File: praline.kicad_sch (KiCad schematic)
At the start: 0 parts

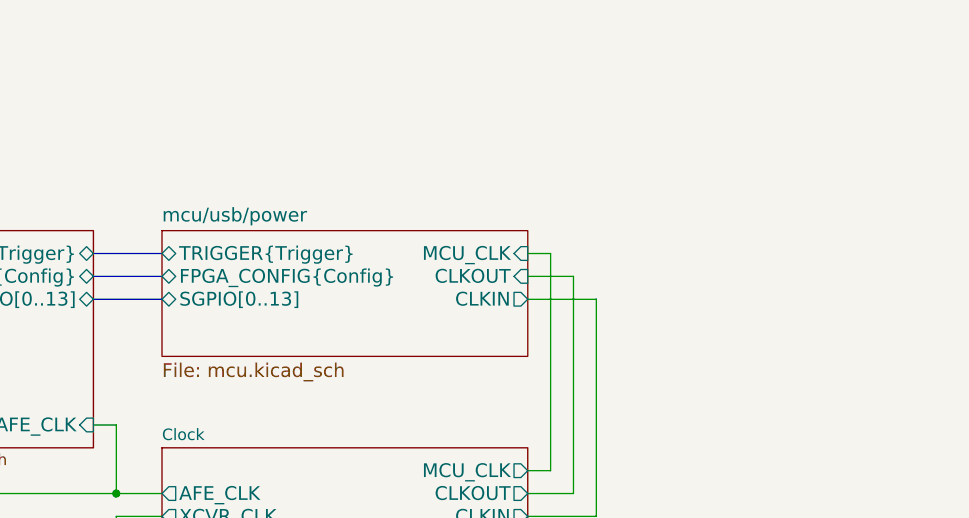
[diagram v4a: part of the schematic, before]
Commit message: Add overvoltage protection
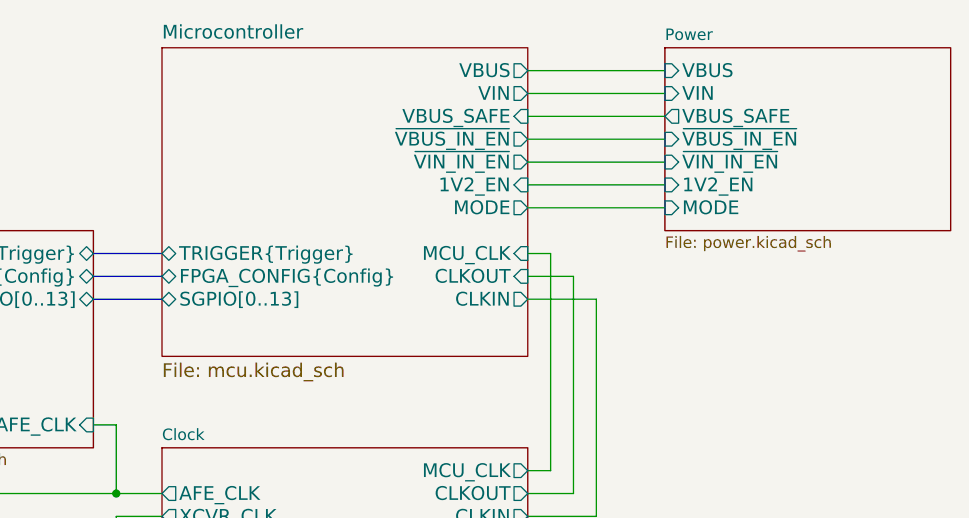
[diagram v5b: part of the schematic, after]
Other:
- sheet mcu/usb/power renamed Microcontroller
- added sheet Power (power.kicad_sch)
- sheet Microcontroller ports: added 1V2_EN, MODE, VBUS, VBUS_SAFE, VIN, ~{VBUS_IN_EN}, ~{VIN_IN_EN}; removed none
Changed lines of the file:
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@@
+		)
+	)
+	(wire
+		(pts
+			(xy 172.72 53.34) (xy 187.96 53.34)
+		)
+		(stroke
+			(width 0)
+			(type default)
 		)
 	)
@@
 	(wire
 		(pts
+			(xy 172.72 43.18) (xy 187.96 43.18)
+		)
+		(stroke
+			(width 0)
+			(type default)
+		)
+	)
+	(wire
+		(pts
 			(xy 172.72 82.55) (xy 175.26 82.55)
 		)
@@
 	(wire
 		(pts
+			(xy 172.72 40.64) (xy 187.96 40.64)
+		)
+		(stroke
+			(width 0)
+			(type default)
+		)
+	)
+	(wire
+		(pts
 			(xy 90.17 114.3) (xy 97.79 114.3)
 		)
@@
 		)
 	)
+	(wire
+		(pts
+			(xy 172.72 45.72) (xy 187.96 45.72)
+		)
+		(stroke
+			(width 0)
+			(type default)
+		)
+	)
 	(bus
 		(pts
@@
 		)
 	)
+	(wire
+		(pts
+			(xy 172.72 50.8) (xy 187.96 50.8)
+		)
+		(stroke
+			(width 0)
+			(type default)
+		)
+	)
+	(wire
+		(pts
+			(xy 172.72 38.1) (xy 187.96 38.1)
+		)
+		(stroke
+			(width 0)
+			(type default)
+		)
+	)
 	(bus
 		(pts
@@
 		)
 	)
+	(wire
+		(pts
+			(xy 172.72 48.26) (xy 187.96 48.26)
+		)
+		(stroke
+			(width 0)
+			(type default)
+		)
+	)
 	(sheet
-		(at 132.08 55.88)
-		(size 40.64 13.97)
+		(at 132.08 35.56)
+		(size 40.64 34.29)
 		(fields_autoplaced yes)
 		(stroke
@@
 			(color 0 0 0 0.0000)
 		)
-		(property "Sheetname" "mcu/usb/power"
-			(at 132.08 55.0414 0)
+		(property "Sheetname" "Microcontroller"
+			(at 132.08 34.7214 0)
 			(effects
 				(font
@@
 		(pin "MCU_CLK" input
 			(at 172.72 58.42 0)
+			(effects
+				(font
+					(size 1.524 1.524)
+				)
+				(justify right)
+			)
+		)
+		(pin "1V2_EN" input
+			(at 172.72 50.8 0)
+			(effects
+				(font
+					(size 1.524 1.524)
+				)
+				(justify right)
+			)
+		)
+		(pin "VBUS" output
+			(at 172.72 38.1 0)
+			(effects
+				(font
+					(size 1.524 1.524)
+				)
+				(justify right)
+			)
+		)
+		(pin "VIN" output
+			(at 172.72 40.64 0)
+			(effects
+				(font
+					(size 1.524 1.524)
+				)
+				(justify right)
+			)
+		)
+		(pin "VBUS_SAFE" input
+			(at 172.72 43.18 0)
+			(effects
+				(font
+					(size 1.524 1.524)
+				)
+				(justify right)
+			)
+		)
+		(pin "~{VBUS_IN_EN}" output
+			(at 172.72 45.72 0)
+			(effects
+				(font
+					(size 1.524 1.524)
+				)
+				(justify right)
+			)
+		)
+		(pin "~{VIN_IN_EN}" output
+			(at 172.72 48.26 0)
+			(effects
+				(font
+					(size 1.524 1.524)
+				)
+				(justify right)
+			)
+		)
+		(pin "MODE" output
+			(at 172.72 53.34 0)
 			(effects
 				(font
@@
 				)
 			)
+		)
+	)
+	(sheet
+		(at 187.96 35.56)
+		(size 31.75 20.32)
+		(fields_autoplaced yes)
+		(stroke
+			(width 0.1524)
+			(type solid)
+		)
+		(fill
+			(color 0 0 0 0.0000)
+		)
+		(property "Sheetname" "Power"
+			(at 187.96 34.8484 0)
+			(effects
+				(font
+					(size 1.27 1.27)
+				)
+				(justify left bottom)
+			)
+		)
+		(property "Sheetfile" "power.kicad_sch"
+			(at 187.96 56.4646 0)
+			(effects
+				(font
+					(size 1.27 1.27)
+				)
+				(justify left top)
+			)
+		)
+		(pin "1V2_EN" input
+			(at 187.96 50.8 180)
+			(effects
+				(font
+					(size 1.524 1.524)
+				)
+				(justify left)
+			)
+		)
+		(pin "~{VBUS_IN_EN}" input
+			(at 187.96 45.72 180)
+			(effects
+				(font
+					(size 1.524 1.524)
+				)
+				(justify left)
+			)
+		)
+		(pin "VBUS" input
+			(at 187.96 38.1 180)
+			(effects
+				(font
+					(size 1.524 1.524)
+				)
+				(justify left)
+			)
+		)
+		(pin "MODE" input
+			(at 187.96 53.34 180)
+			(effects
+				(font
+					(size 1.524 1.524)
+				)
+				(justify left)
+			)
+		)
+		(pin "~{VIN_IN_EN}" input
+			(at 187.96 48.26 180)
+			(effects
+				(font
+					(size 1.524 1.524)
+				)
+				(justify left)
+			)
+		)
+		(pin "VIN" input
+			(at 187.96 40.64 180)
+			(effects
+				(font
+					(size 1.524 1.524)
+				)
+				(justify left)
+			)
+		)
+		(pin "VBUS_SAFE" output
+			(at 187.96 43.18 180)
+			(effects
+				(font
+					(size 1.524 1.524)
+				)
+				(justify left)
+			)
+		)
+		(instances
+			(project "praline"
+				(path "/dba4afc6-760f-46cb-a936-032b76448f03"
+					(page "9")
+				)
+			)

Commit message: Add more expansion pins
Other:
- sheet Clock ports: added AUX_CLK; removed none
- sheet Microcontroller ports: added AUX_CLK; removed none
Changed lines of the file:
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@@
+	(wire
+		(pts
+			(xy 182.88 66.04) (xy 182.88 90.17)
+		)
+		(stroke
+			(width 0)
+			(type default)
+		)
+	)
 	(wire
 		(pts
@@
 		(pts
 			(xy 124.46 58.42) (xy 132.08 58.42)
+		)
+		(stroke
+			(width 0)
+			(type default)
+		)
+	)
+	(wire
+		(pts
+			(xy 172.72 66.04) (xy 182.88 66.04)
+		)
+		(stroke
+			(width 0)
+			(type default)
+		)
+	)
+	(wire
+		(pts
+			(xy 182.88 90.17) (xy 172.72 90.17)
 		)
 		(stroke
@@
 			)
 		)
+		(pin "AUX_CLK" input
+			(at 172.72 66.04 0)
+			(effects
+				(font
+					(size 1.524 1.524)
+				)
+				(justify right)
+			)
+		)
 		(instances
 			(project "praline"
@@
 			(effects
 				(font
+					(size 1.524 1.524)
+				)
+				(justify right)
+			)
+		)
+		(pin "AUX_CLK" output
+			(at 172.72 90.17 0)
+			(effects
+				(font

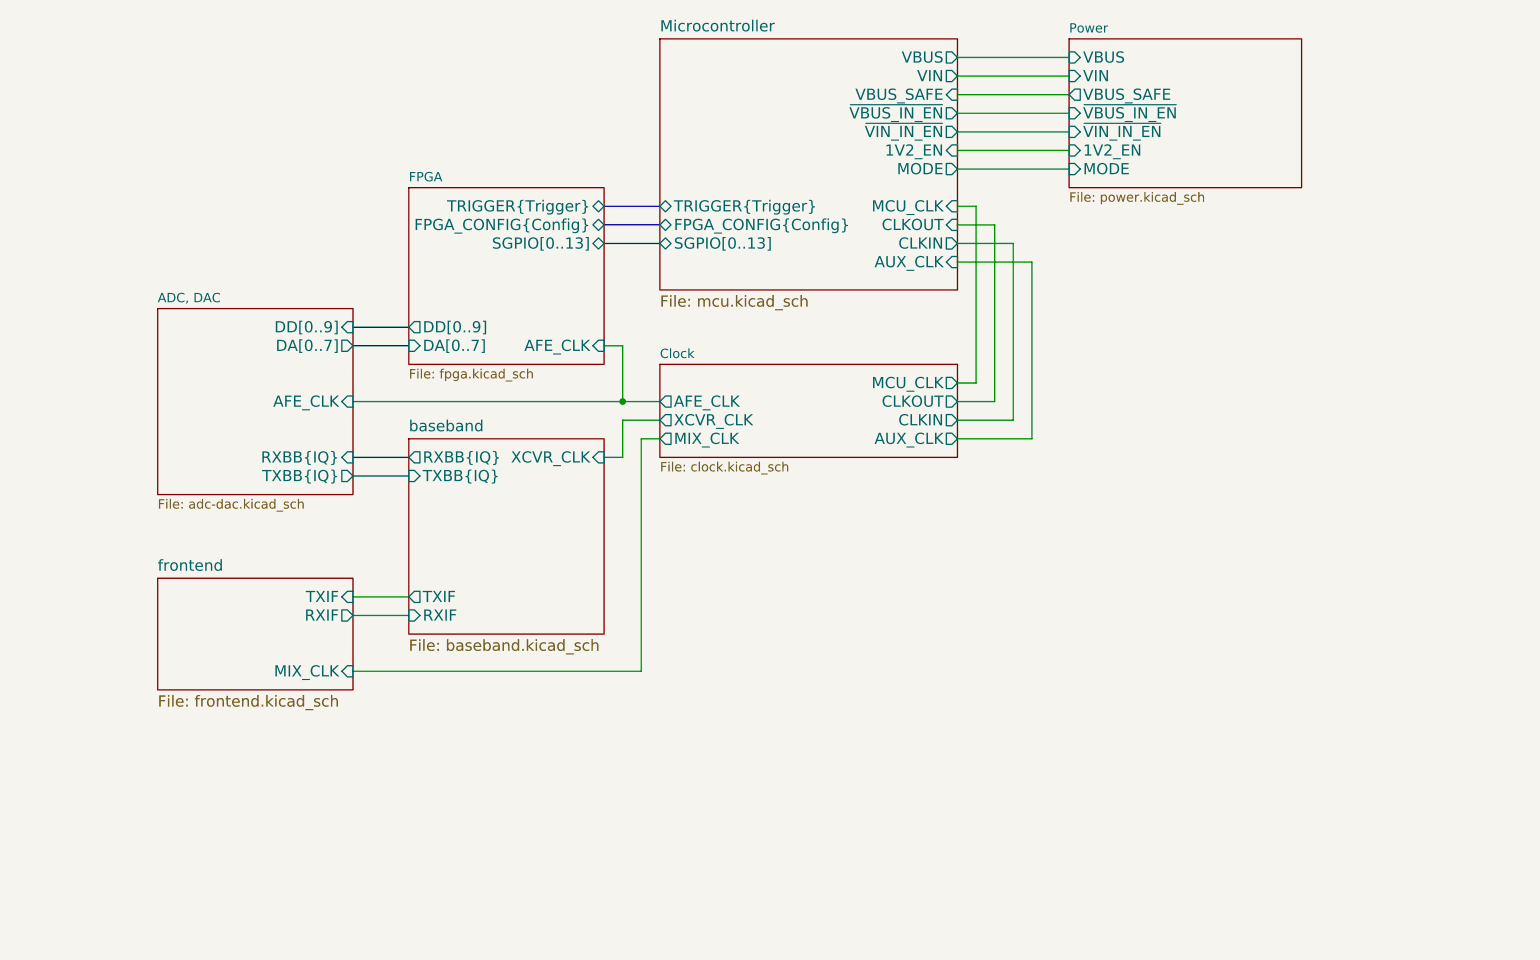
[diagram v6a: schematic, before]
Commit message: Rearrange RF section
- Use DPDT RF switches to reduce long tracks
- Add limiter
- Add switch control logic
- Move ADC/DAC U18 to RF area
- Remove baseband header P9
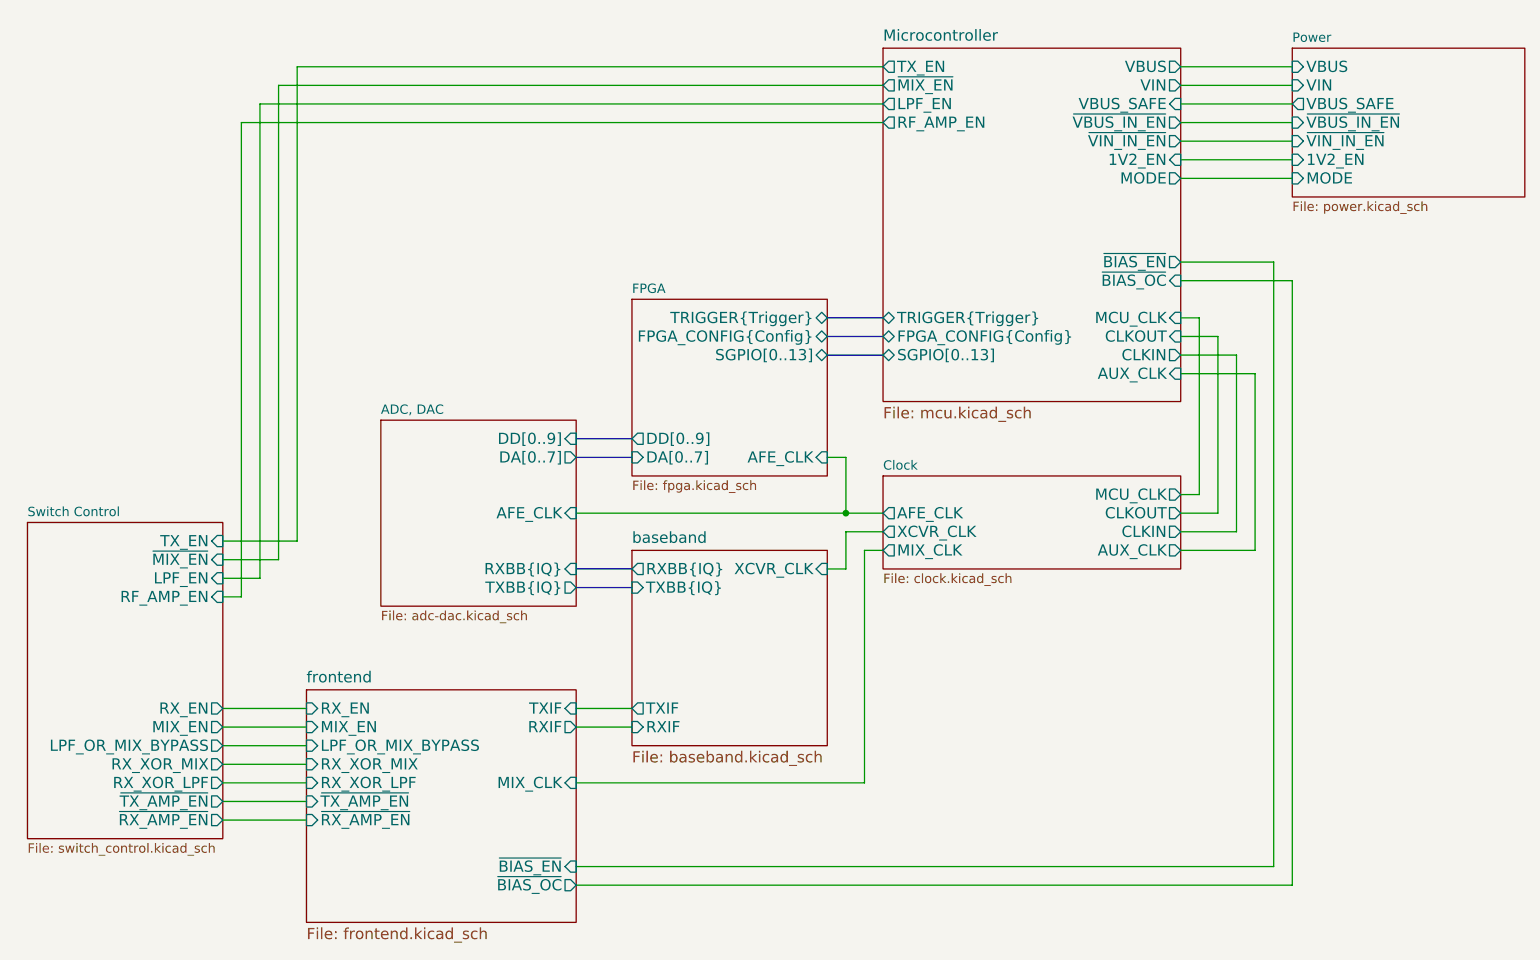
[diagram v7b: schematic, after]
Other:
- added sheet Switch Control (switch_control.kicad_sch)
- sheet Microcontroller ports: added LPF_EN, RF_AMP_EN, TX_EN, ~{BIAS_EN}, ~{BIAS_OC}, ~{MIX_EN}; removed none
- sheet frontend ports: added LPF_OR_MIX_BYPASS, MIX_EN, RX_EN, RX_XOR_LPF, RX_XOR_MIX, ~{BIAS_EN}, ~{BIAS_OC}, ~{RX_AMP_EN}, ~{TX_AMP_EN}; removed none

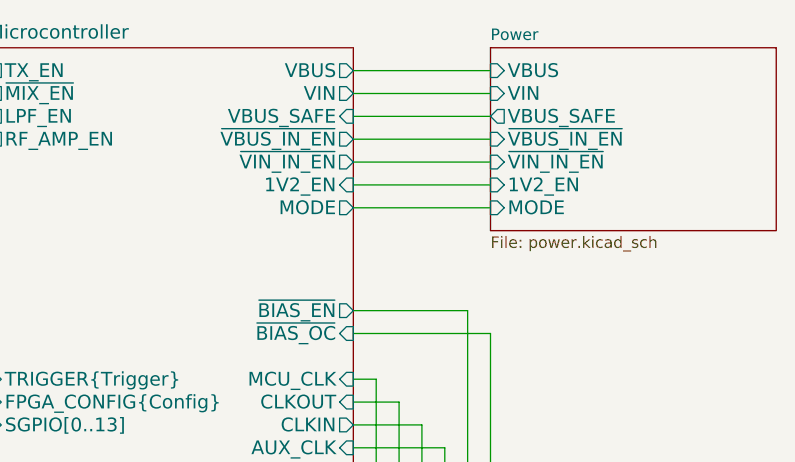
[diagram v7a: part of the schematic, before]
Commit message: Add current-limiting switch to expansion interface
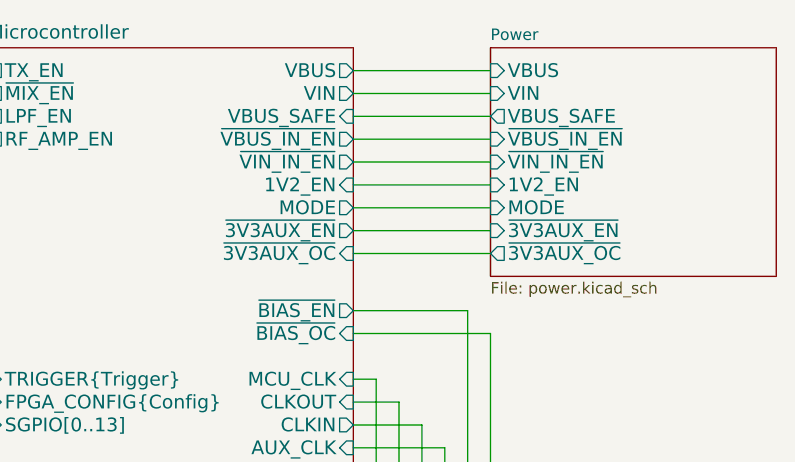
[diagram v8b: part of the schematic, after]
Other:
- sheet Microcontroller ports: added ~{3V3AUX_EN}, ~{3V3AUX_OC}; removed none
- sheet Power ports: added ~{3V3AUX_EN}, ~{3V3AUX_OC}; removed none
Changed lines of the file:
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@@
+	(wire
+		(pts
+			(xy 203.2 57.15) (xy 218.44 57.15)
+		)
+		(stroke
+			(width 0)
+			(type default)
+		)
+	)
 	(wire
 		(pts
@@
 		(pts
 			(xy 72.39 132.08) (xy 83.82 132.08)
+		)
+		(stroke
+			(width 0)
+			(type default)
+		)
+	)
+	(wire
+		(pts
+			(xy 203.2 59.69) (xy 218.44 59.69)
 		)
 		(stroke
@@
 			)
 		)
+		(pin "~{3V3AUX_EN}" output
+			(at 203.2 57.15 0)
+			(effects
+				(font
+					(size 1.524 1.524)
+				)
+				(justify right)
+			)
+		)
+		(pin "~{3V3AUX_OC}" input
+			(at 203.2 59.69 0)
+			(effects
+				(font
+					(size 1.524 1.524)
+				)
+				(justify right)
+			)
+		)
 		(instances
 			(project "praline"
@@
 	(sheet
 		(at 218.44 36.83)
-		(size 31.75 20.32)
+		(size 31.75 25.4)
 		(fields_autoplaced yes)
 		(stroke
@@
 		)
 		(property "Sheetfile" "power.kicad_sch"
-			(at 218.44 57.7346 0)
+			(at 218.44 62.8146 0)
 			(effects
 				(font
@@
 			(effects
 				(font
+					(size 1.524 1.524)
+				)
+				(justify left)
+			)
+		)
+		(pin "~{3V3AUX_EN}" input
+			(at 218.44 57.15 180)
+			(effects
+				(font
+					(size 1.524 1.524)
+				)
+				(justify left)
+			)
+		)
+		(pin "~{3V3AUX_OC}" output
+			(at 218.44 59.69 180)
+			(effects
+				(font
